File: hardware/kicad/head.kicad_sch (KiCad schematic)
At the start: 4 parts, among them U5 XIAO ESP32-S3, U6 left eye GC9A01, U7 right eye GC9A01, U8 mouth OLED 2.08in SH1122

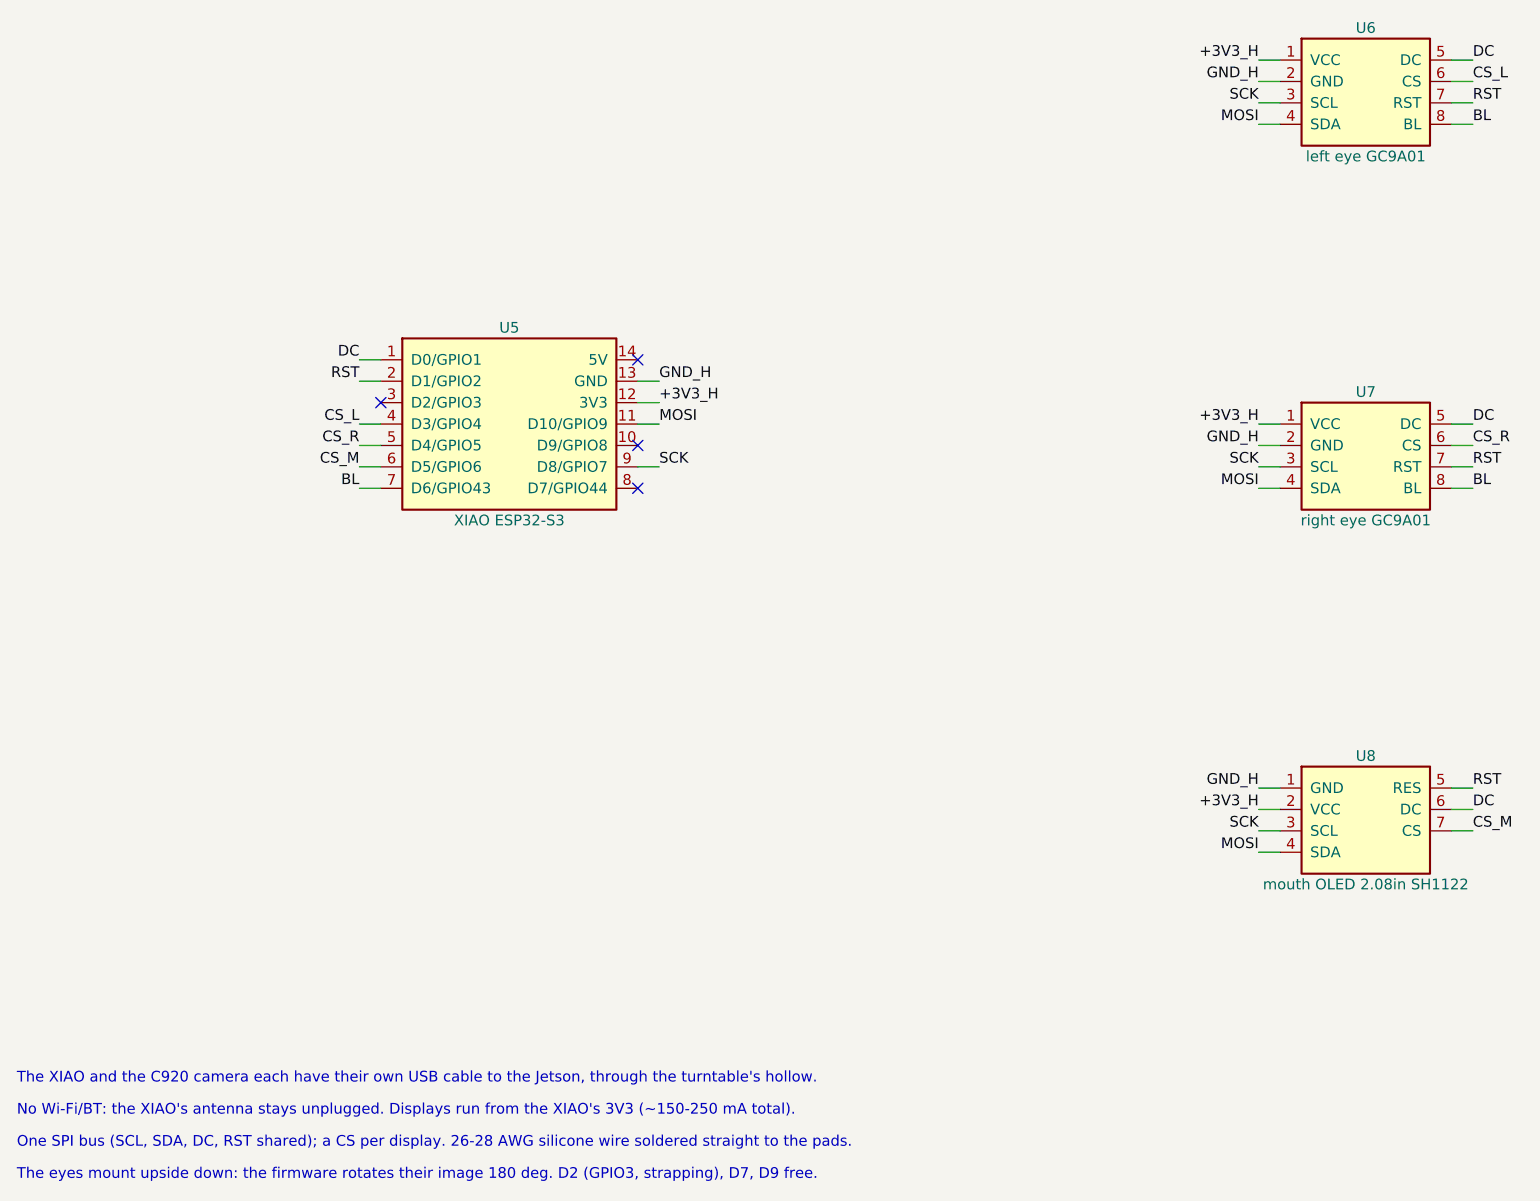
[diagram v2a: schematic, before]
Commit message: Measured parts: panel jack (11.2 mm thread -> 11.5 hole), GC9A01 eyes (37.8 board, 3.8 thick, 7 pins, no BL)
Co-Authored-By: Claude Opus 5.5 <noreply@anthropic.com>
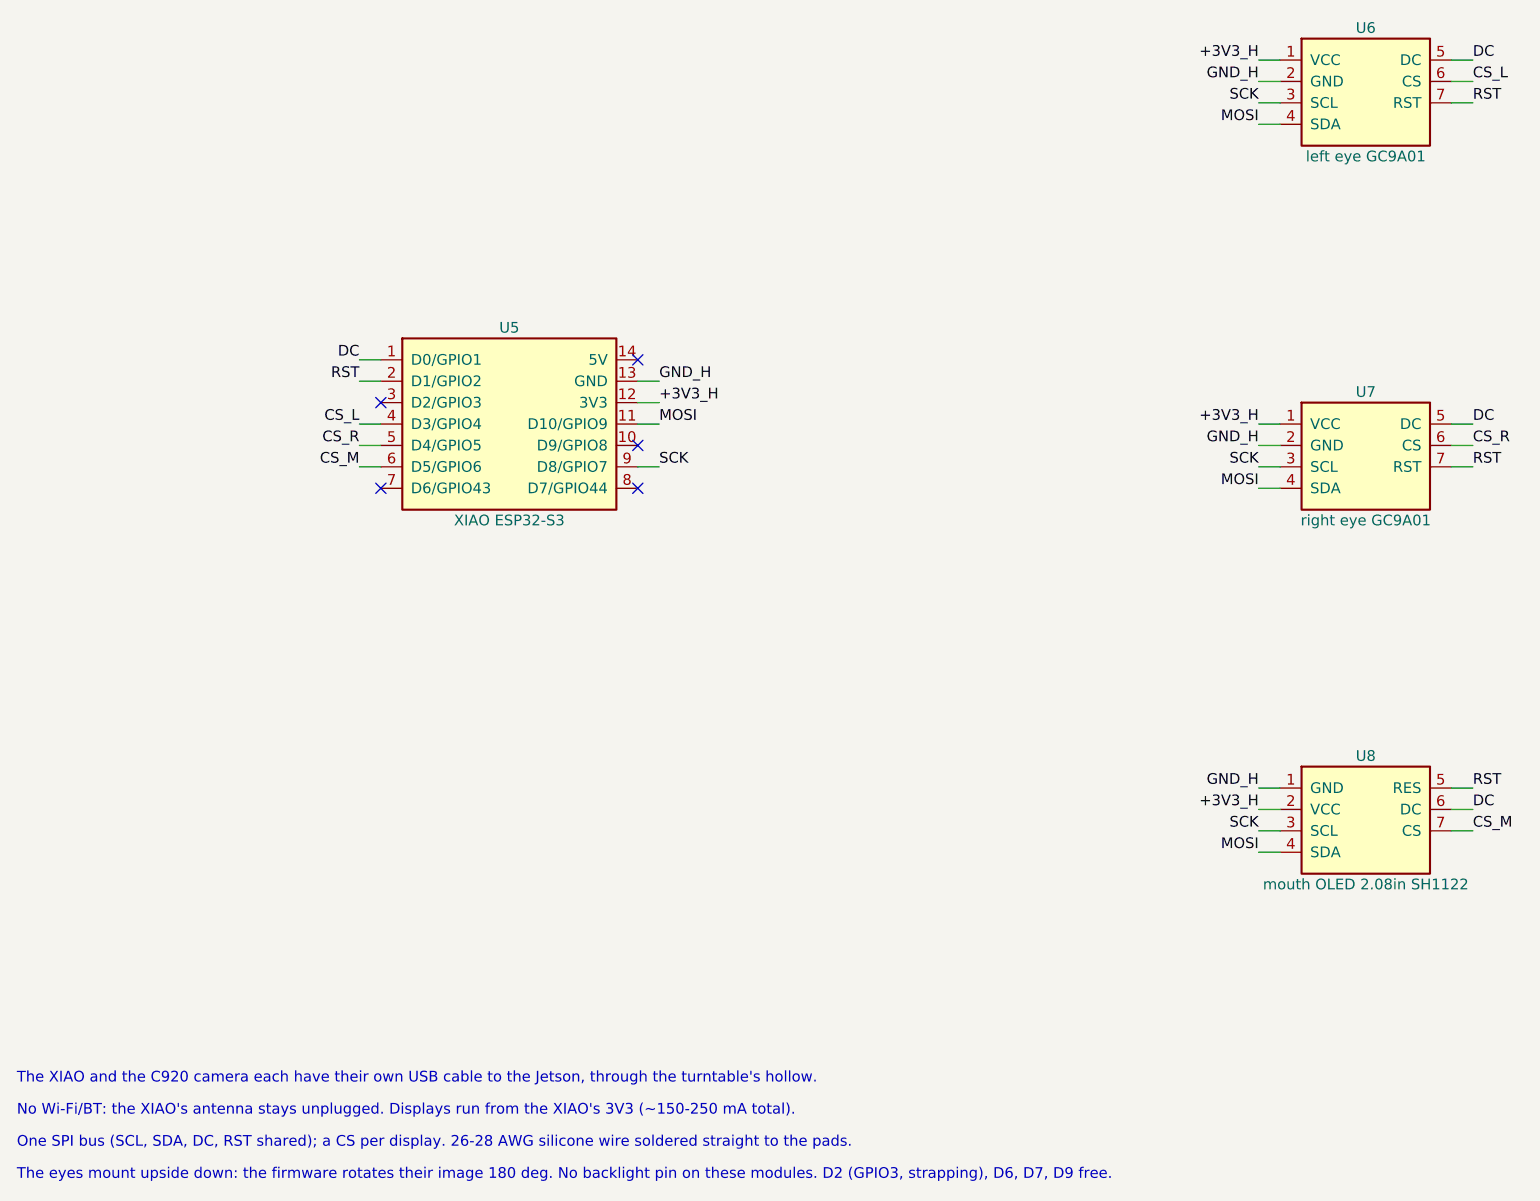
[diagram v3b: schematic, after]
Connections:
- removed net BL: U5.7 (D6/GPIO43), U6.8 (BL), U7.8 (BL)
- no-connect marks 4 -> 5
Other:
- note added: "The eyes mount upside down: the firmware rotates their image 180 deg. No backlight pin on these modules. D2 (GPIO3, strapping), D6, D7, D9 free."
- note removed: "The eyes mount upside down: the firmware rotates their image 180 deg. D2 (GPIO3, strapping), D7, D9 free."
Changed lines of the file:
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@@
 (wire (pts (xy 63.5 106.68) (xy 60.96 106.68)) (stroke (width 0) (type default)))
 (label "CS_M" (at 60.96 106.68 180) (effects (font (size 1.27 1.27)) (justify right bottom)))
-(wire (pts (xy 63.5 109.22) (xy 60.96 109.22)) (stroke (width 0) (type default)))
-(label "BL" (at 60.96 109.22 180) (effects (font (size 1.27 1.27)) (justify right bottom)))
+(no_connect (at 63.5 109.22))
 (no_connect (at 93.98 93.98))
 (wire (pts (xy 93.98 96.52) (xy 96.52 96.52)) (stroke (width 0) (type default)))
@@
 (pin "6")
 (pin "7")
-(pin "8")
 (instances (project "piper-watch" (path "/833d4739-1417-5dca-9991-7683c6f341a1/fc0de084-d5c1-5c02-9a61-96fcb8a58256" (reference "U6") (unit 1)))))
 (wire (pts (xy 170.18 58.42) (xy 167.64 58.42)) (stroke (width 0) (type default)))
@@
 (wire (pts (xy 190.5 63.5) (xy 193.04 63.5)) (stroke (width 0) (type default)))
 (label "RST" (at 193.04 63.5 0) (effects (font (size 1.27 1.27)) (justify left bottom)))
-(wire (pts (xy 190.5 66.04) (xy 193.04 66.04)) (stroke (width 0) (type default)))
-(label "BL" (at 193.04 66.04 0) (effects (font (size 1.27 1.27)) (justify left bottom)))
 (symbol (lib_id "piper-watch:GC9A01_Module") (at 180.34 106.68 0) (unit 1) (exclude_from_sim no) (in_bom yes) (on_board no) (dnp no)
 (property "Reference" "U7" (at 180.34 97.79 0) (effects (font (size 1.27 1.27))))
@@
 (pin "6")
 (pin "7")
-(pin "8")
 (instances (project "piper-watch" (path "/833d4739-1417-5dca-9991-7683c6f341a1/fc0de084-d5c1-5c02-9a61-96fcb8a58256" (reference "U7") (unit 1)))))
 (wire (pts (xy 170.18 101.6) (xy 167.64 101.6)) (stroke (width 0) (type default)))
@@
 (wire (pts (xy 190.5 106.68) (xy 193.04 106.68)) (stroke (width 0) (type default)))
 (label "RST" (at 193.04 106.68 0) (effects (font (size 1.27 1.27)) (justify left bottom)))
-(wire (pts (xy 190.5 109.22) (xy 193.04 109.22)) (stroke (width 0) (type default)))
-(label "BL" (at 193.04 109.22 0) (effects (font (size 1.27 1.27)) (justify left bottom)))
 (symbol (lib_id "piper-watch:SH1122_OLED") (at 180.34 149.86 0) (unit 1) (exclude_from_sim no) (in_bom yes) (on_board no) (dnp no)
 (property "Reference" "U8" (at 180.34 140.97 0) (effects (font (size 1.27 1.27))))
@@
 (text "No Wi-Fi/BT: the XIAO's antenna stays unplugged. Displays run from the XIAO's 3V3 (~150-250 mA total)." (exclude_from_sim no) (at 20.32 183.81 0) (effects (font (size 1.27 1.27)) (justify left bottom)))
 (text "One SPI bus (SCL, SDA, DC, RST shared); a CS per display. 26-28 AWG silicone wire soldered straight to the pads." (exclude_from_sim no) (at 20.32 187.62 0) (effects (font (size 1.27 1.27)) (justify left bottom)))
-(text "The eyes mount upside down: the firmware rotates their image 180 deg. D2 (GPIO3, strapping), D7, D9 free." (exclude_from_sim no) (at 20.32 191.43 0) (effects (font (size 1.27 1.27)) (justify left bottom)))
+(text "The eyes mount upside down: the firmware rotates their image 180 deg. No backlight pin on these modules. D2 (GPIO3, strapping), D6, D7, D9 free." (exclude_from_sim no) (at 20.32 191.43 0) (effects (font (size 1.27 1.27)) (justify left bottom)))
 (embedded_fonts no))
